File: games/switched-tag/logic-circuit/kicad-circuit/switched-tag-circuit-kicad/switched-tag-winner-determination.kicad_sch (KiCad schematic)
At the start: 6 parts

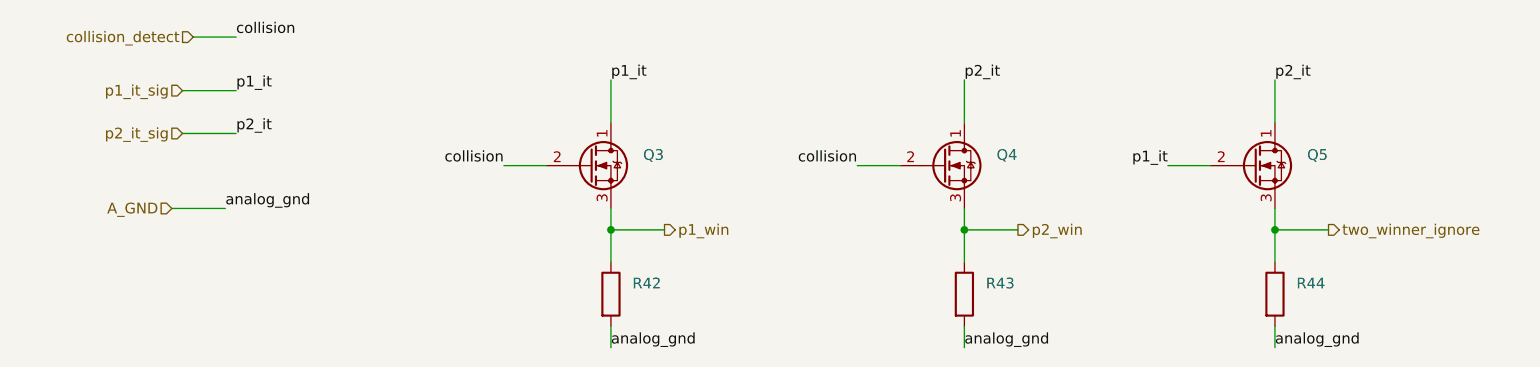
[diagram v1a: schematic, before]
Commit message: Updated kicad circuit. The kicad sim and ltspice do not match up well. Need to fix.
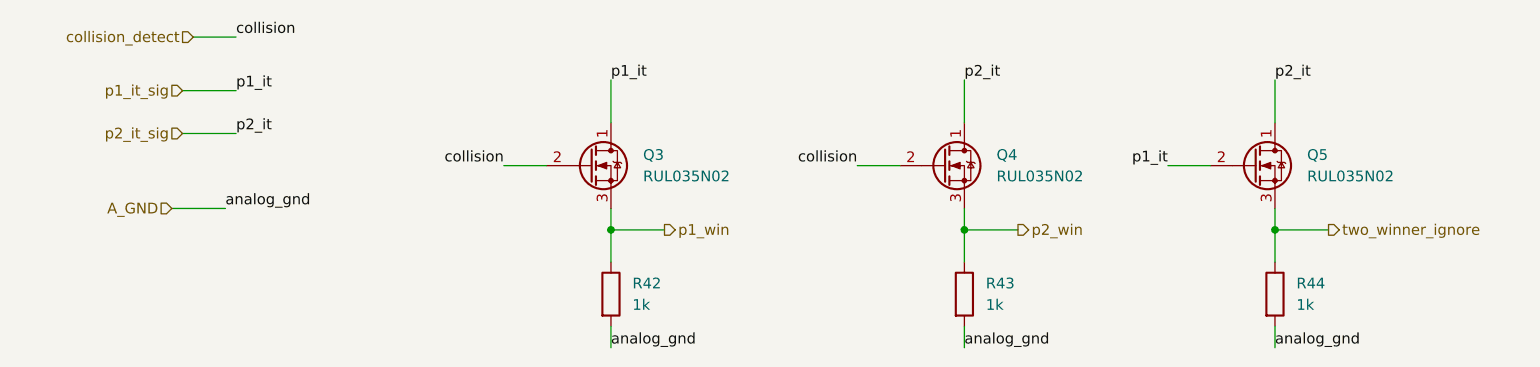
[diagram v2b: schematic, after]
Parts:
- Q3, Q4, Q5: value (none) -> RUL035N02
- R42, R43, R44: value (none) -> 1k
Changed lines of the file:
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@@
       (effects (font (size 1.27 1.27)) (justify left))
     )
-    (property "Value" "" (id 1) (at 116.84 123.1899 0)
+    (property "Value" "1k" (id 1) (at 116.84 123.1899 0)
       (effects (font (size 1.27 1.27)) (justify left))
     )
@@
       (effects (font (size 1.27 1.27)) (justify left))
     )
-    (property "Value" "" (id 1) (at 158.75 123.1899 0)
+    (property "Value" "1k" (id 1) (at 158.75 123.1899 0)
       (effects (font (size 1.27 1.27)) (justify left))
     )
@@
       (effects (font (size 1.27 1.27)) (justify left))
     )
-    (property "Value" "" (id 1) (at 118.11 107.9499 0)
+    (property "Value" "RUL035N02" (id 1) (at 118.11 107.9499 0)
       (effects (font (size 1.27 1.27)) (justify left))
     )
@@
       (effects (font (size 1.27 1.27)) (justify left))
     )
-    (property "Value" "" (id 1) (at 195.58 123.1899 0)
+    (property "Value" "1k" (id 1) (at 195.58 123.1899 0)
       (effects (font (size 1.27 1.27)) (justify left))
     )
@@
       (effects (font (size 1.27 1.27)) (justify left))
     )
-    (property "Value" "" (id 1) (at 196.85 107.9499 0)
+    (property "Value" "RUL035N02" (id 1) (at 196.85 107.9499 0)
       (effects (font (size 1.27 1.27)) (justify left))
     )
@@
       (effects (font (size 1.27 1.27)) (justify left))
     )
-    (property "Value" "" (id 1) (at 160.02 107.9499 0)
+    (property "Value" "RUL035N02" (id 1) (at 160.02 107.9499 0)
       (effects (font (size 1.27 1.27)) (justify left))
     )

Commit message: Added some prep work for console hardware.
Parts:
- Q3, Q4, Q5: value RUL035N02 -> (none); Spice_Lib_File /home/pab/Inventions/analog-circuit-game-console/ms-circuit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 -> ../../../../../spice-models/rul035n02.lib
- R42, R43, R44: value 1k -> (none)
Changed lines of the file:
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@@
       (effects (font (size 1.27 1.27)) (justify left))
     )
-    (property "Value" "1k" (id 1) (at 116.84 123.1899 0)
+    (property "Value" "" (id 1) (at 116.84 123.1899 0)
       (effects (font (size 1.27 1.27)) (justify left))
     )
@@
       (effects (font (size 1.27 1.27)) (justify left))
     )
-    (property "Value" "1k" (id 1) (at 158.75 123.1899 0)
+    (property "Value" "" (id 1) (at 158.75 123.1899 0)
       (effects (font (size 1.27 1.27)) (justify left))
     )
@@
       (effects (font (size 1.27 1.27)) (justify left))
     )
-    (property "Value" "RUL035N02" (id 1) (at 118.11 107.9499 0)
+    (property "Value" "" (id 1) (at 118.11 107.9499 0)
       (effects (font (size 1.27 1.27)) (justify left))
     )
@@
       (effects (font (size 1.27 1.27)) hide)
     )
-    (property "Spice_Lib_File" "/home/pab/Inventions/analog-circuit-game-console/ms-circuit-video-games/spice-models/rul035n02.lib" (id 7) (at 111.76 106.68 0)
+    (property "Spice_Lib_File" "../../../../../spice-models/rul035n02.lib" (id 7) (at 111.76 106.68 0)
       (effects (font (size 1.27 1.27)) hide)
     )
@@
       (effects (font (size 1.27 1.27)) (justify left))
     )
-    (property "Value" "1k" (id 1) (at 195.58 123.1899 0)
+    (property "Value" "" (id 1) (at 195.58 123.1899 0)
       (effects (font (size 1.27 1.27)) (justify left))
     )
@@
       (effects (font (size 1.27 1.27)) (justify left))
     )
-    (property "Value" "RUL035N02" (id 1) (at 196.85 107.9499 0)
+    (property "Value" "" (id 1) (at 196.85 107.9499 0)
       (effects (font (size 1.27 1.27)) (justify left))
     )
@@
       (effects (font (size 1.27 1.27)) hide)
     )
-    (property "Spice_Lib_File" "/home/pab/Inventions/analog-circuit-game-console/ms-circuit-video-games/spice-models/rul035n02.lib" (id 7) (at 190.5 106.68 0)
+    (property "Spice_Lib_File" "../../../../../spice-models/rul035n02.lib" (id 7) (at 190.5 106.68 0)
       (effects (font (size 1.27 1.27)) hide)
     )
@@
       (effects (font (size 1.27 1.27)) (justify left))
     )
-    (property "Value" "RUL035N02" (id 1) (at 160.02 107.9499 0)
+    (property "Value" "" (id 1) (at 160.02 107.9499 0)
       (effects (font (size 1.27 1.27)) (justify left))
     )
@@
       (effects (font (size 1.27 1.27)) hide)
     )
-    (property "Spice_Lib_File" "/home/pab/Inventions/analog-circuit-game-console/ms-circuit-video-games/spice-models/rul035n02.lib" (id 7) (at 153.67 106.68 0)
+    (property "Spice_Lib_File" "../../../../../spice-models/rul035n02.lib" (id 7) (at 153.67 106.68 0)
       (effects (font (size 1.27 1.27)) hide)
     )
